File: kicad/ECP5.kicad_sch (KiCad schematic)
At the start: 4 parts

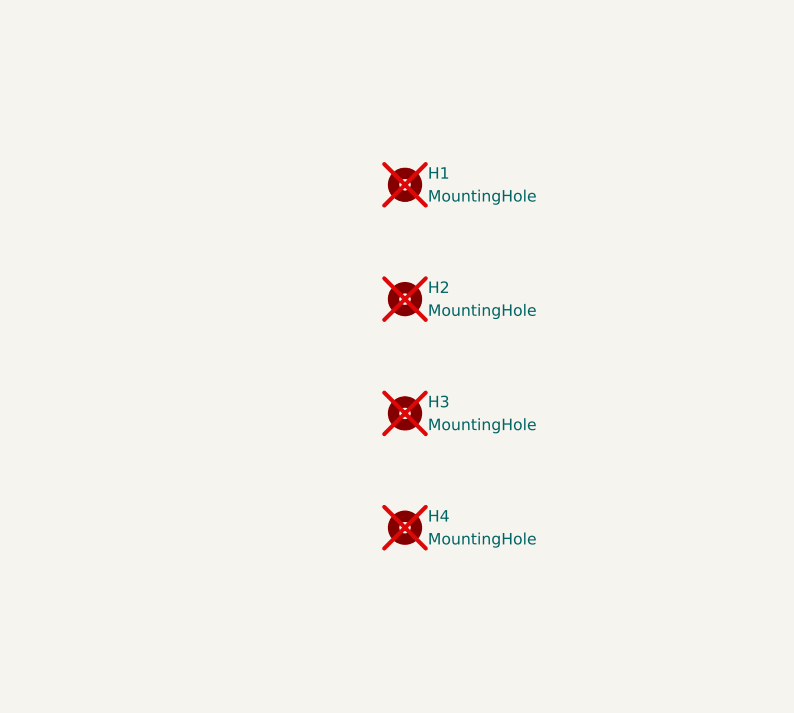
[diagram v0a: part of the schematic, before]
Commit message: First pass at arranging components
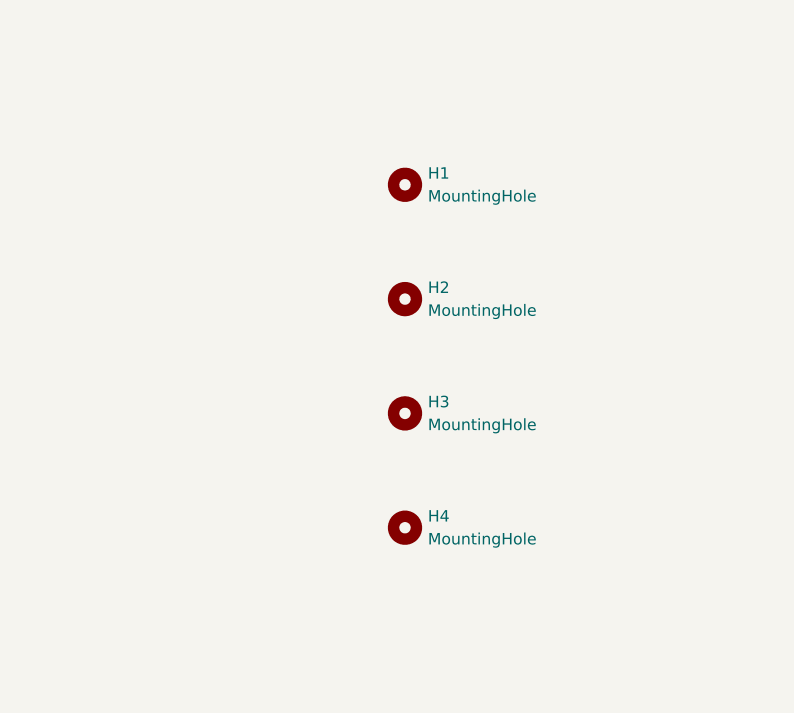
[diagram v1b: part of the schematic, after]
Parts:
- H1, H2, H3, H4: now fitted
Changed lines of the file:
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@@
 		(in_bom no)
 		(on_board yes)
-		(dnp yes)
+		(dnp no)
 		(fields_autoplaced yes)
 		(property "Reference" "H4"
@@
 		(in_bom no)
 		(on_board yes)
-		(dnp yes)
+		(dnp no)
 		(fields_autoplaced yes)
 		(property "Reference" "H1"
@@
 		(in_bom no)
 		(on_board yes)
-		(dnp yes)
+		(dnp no)
 		(fields_autoplaced yes)
 		(property "Reference" "H2"
@@
 		(in_bom no)
 		(on_board yes)
-		(dnp yes)
+		(dnp no)
 		(fields_autoplaced yes)
 		(property "Reference" "H3"
